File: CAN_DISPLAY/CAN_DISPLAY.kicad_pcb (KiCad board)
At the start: 4 copper layers, 188 x 103 mm, 130 parts, among them J1 DISPLAY, J10 DCDC 5V 3A, J11 Micro_SD_Card, J13 Prodrammer, J14 Display, J15 LED Display, J16 BME280 Module, J18 J-Link, J19 TSL2561, J2 I2C Sensor 1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

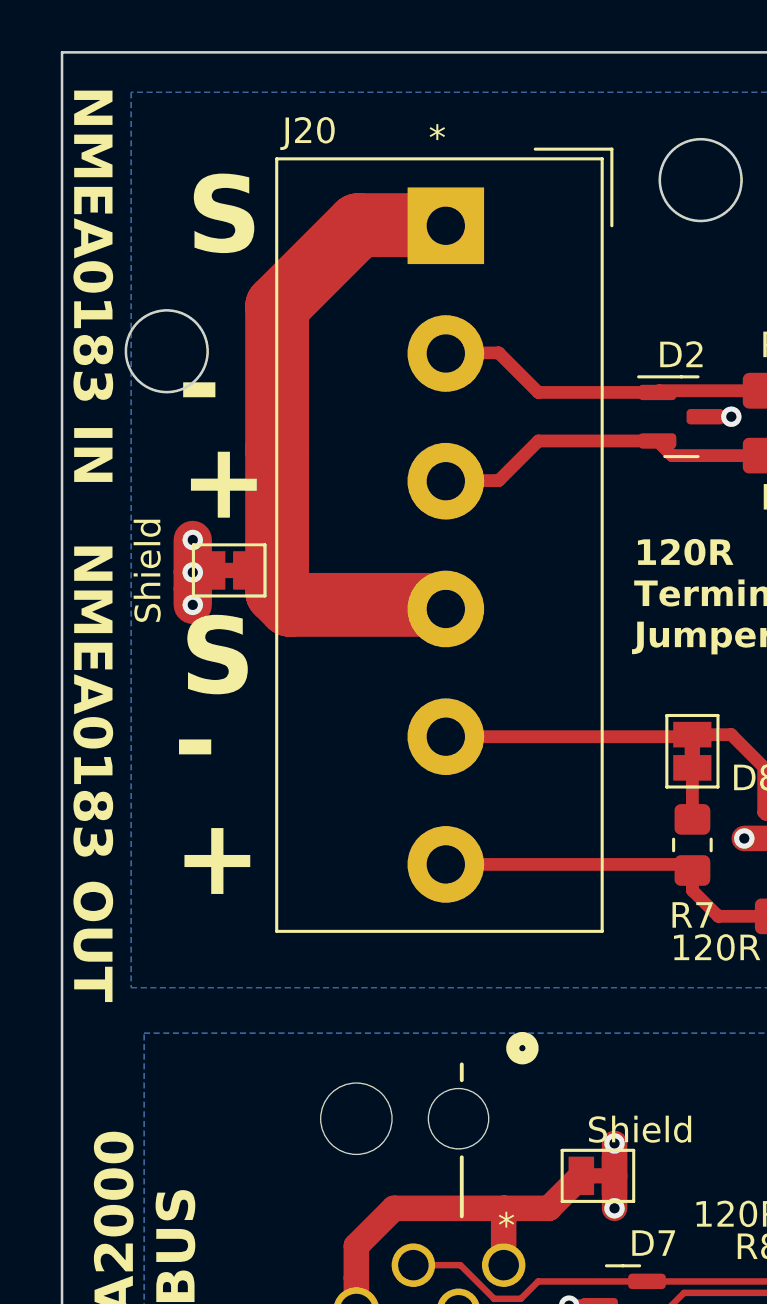
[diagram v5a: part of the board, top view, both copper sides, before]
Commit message: Added Board Test
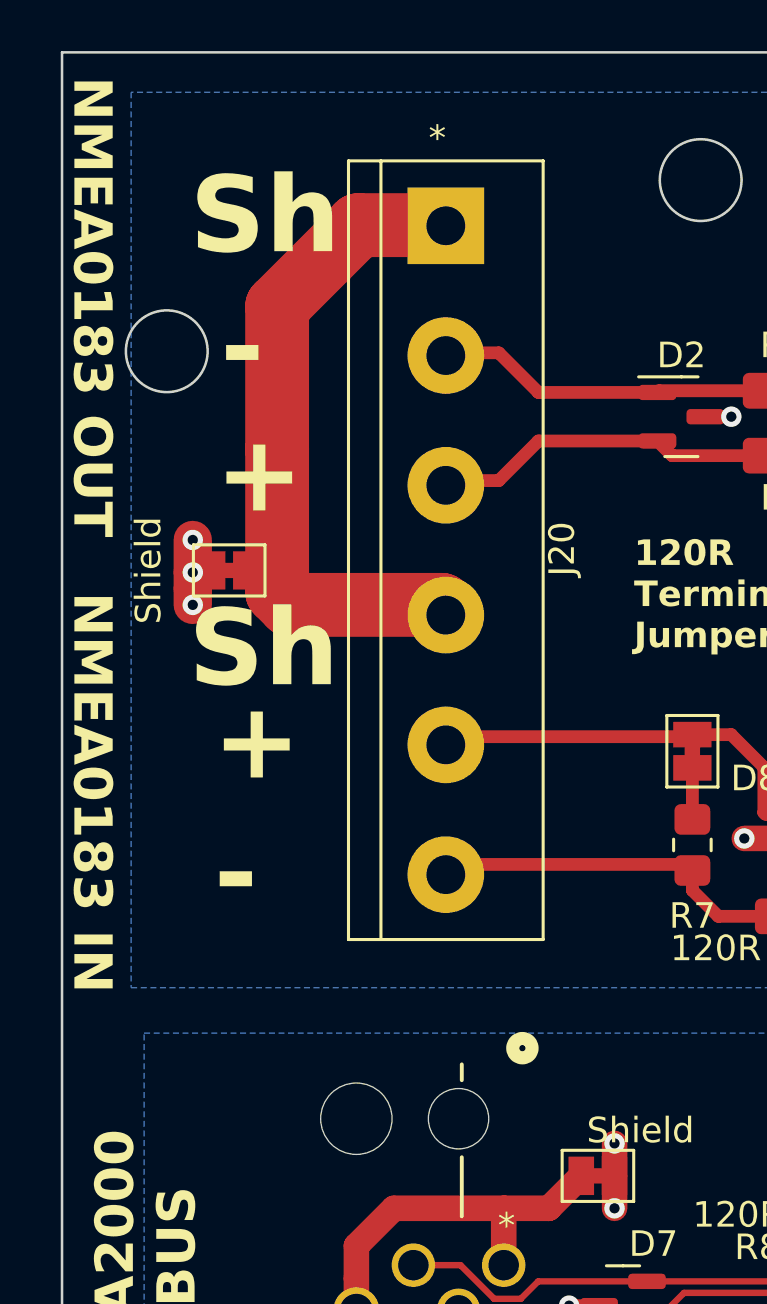
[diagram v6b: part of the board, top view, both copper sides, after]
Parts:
- J20: footprint TerminalBlock_Altech:Altech_AK300_1x06_P5.00mm_45-Degree -> TerminalBlock:TerminalBlock_bornier-6_P5.08mm
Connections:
- net Net-(U5-A) renamed /Isolated/rNMEA IN-
- net Net-(U5-B) renamed /Isolated/rNMEA IN+
- net Net-(U5-Y) renamed /Isolated/rNMEA OUT-
- net Net-(U5-Z) renamed /Isolated/rNMEA OUT+
- D2 pad 1: /Isolated/NMEA IN- -> /Isolated/NMEA OUT-
- D2 pad 2: /Isolated/NMEA IN+ -> /Isolated/NMEA OUT+
- D8 pad 1: /Isolated/NMEA OUT+ -> /Isolated/NMEA IN-
- D8 pad 2: /Isolated/NMEA OUT- -> /Isolated/NMEA IN+
- J20 pad 2: /Isolated/NMEA IN- -> /Isolated/NMEA OUT-
- J20 pad 3: /Isolated/NMEA IN+ -> /Isolated/NMEA OUT+
- J20 pad 5: /Isolated/NMEA OUT- -> /Isolated/NMEA IN+
- J20 pad 6: /Isolated/NMEA OUT+ -> /Isolated/NMEA IN-
- JP18 pad 2: /Isolated/NMEA OUT- -> /Isolated/NMEA IN+
- R1 pad 2: /Isolated/NMEA OUT- -> /Isolated/NMEA IN+
- R2 pad 2: /Isolated/NMEA OUT+ -> /Isolated/NMEA IN-
- R3 pad 2: /Isolated/NMEA IN+ -> /Isolated/NMEA OUT+
- R4 pad 2: /Isolated/NMEA IN- -> /Isolated/NMEA OUT-
- R5 pad 2: /Isolated/NMEA OUT- -> /Isolated/NMEA IN+
- R6 pad 1: /Isolated/NMEA OUT+ -> /Isolated/NMEA IN-
- R7 pad 2: /Isolated/NMEA OUT+ -> /Isolated/NMEA IN-
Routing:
- net /Isolated/NMEA OUT-: track 33.8 -> 13.0 mm
- net /Isolated/NMEA IN+: track 13.1 -> 33.8 mm
- net /Isolated/NMEA IN-: track 13.0 -> 32.3 mm
- net /Isolated/NMEA OUT+: track 32.3 -> 13.1 mm
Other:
- board text added: "NMEA0183 OUT NMEA0183 IN"
- board text added: "Sh"
- board text removed: "NMEA0183 IN NMEA0183 OUT"
- board text removed: "S"

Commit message: 1234
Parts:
- J20: footprint TerminalBlock:TerminalBlock_bornier-6_P5.08mm -> TerminalBlock_Altech:Altech_AK300_1x06_P5.00mm_45-Degree
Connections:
- net /Isolated/rNMEA IN+ renamed Net-(U5-B)
- net /Isolated/rNMEA IN- renamed Net-(U5-A)
- net /Isolated/rNMEA OUT+ renamed Net-(U5-Z)
- net /Isolated/rNMEA OUT- renamed Net-(U5-Y)
- D2 pad 1: /Isolated/NMEA OUT- -> /Isolated/NMEA IN-
- D2 pad 2: /Isolated/NMEA OUT+ -> /Isolated/NMEA IN+
- D8 pad 1: /Isolated/NMEA IN- -> /Isolated/NMEA OUT+
- D8 pad 2: /Isolated/NMEA IN+ -> /Isolated/NMEA OUT-
- J20 pad 2: /Isolated/NMEA OUT- -> /Isolated/NMEA IN-
- J20 pad 3: /Isolated/NMEA OUT+ -> /Isolated/NMEA IN+
- J20 pad 5: /Isolated/NMEA IN+ -> /Isolated/NMEA OUT-
- J20 pad 6: /Isolated/NMEA IN- -> /Isolated/NMEA OUT+
- JP18 pad 2: /Isolated/NMEA IN+ -> /Isolated/NMEA OUT-
- R1 pad 2: /Isolated/NMEA IN+ -> /Isolated/NMEA OUT-
- R2 pad 2: /Isolated/NMEA IN- -> /Isolated/NMEA OUT+
- R3 pad 2: /Isolated/NMEA OUT+ -> /Isolated/NMEA IN+
- R4 pad 2: /Isolated/NMEA OUT- -> /Isolated/NMEA IN-
- R5 pad 2: /Isolated/NMEA IN+ -> /Isolated/NMEA OUT-
- R6 pad 1: /Isolated/NMEA IN- -> /Isolated/NMEA OUT+
- R7 pad 2: /Isolated/NMEA IN- -> /Isolated/NMEA OUT+
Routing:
- net /Isolated/NMEA OUT-: track 13.0 -> 33.8 mm
- net /Isolated/NMEA IN+: track 33.8 -> 13.1 mm
- net /Isolated/NMEA IN-: track 32.3 -> 13.0 mm
- net /Isolated/NMEA OUT+: track 13.1 -> 32.3 mm
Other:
- board text added: "NMEA0183 IN NMEA0183 OUT"
- board text added: "S"
- board text removed: "NMEA0183 OUT NMEA0183 IN"
- board text removed: "Sh"
